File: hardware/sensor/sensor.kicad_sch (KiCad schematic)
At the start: 35 parts, among them IC1 ATTINY202-SSN, IC2 Si4012-C1001GTR, IC3 TPS3839L30DBZR, J1 M20-9770342

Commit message: EG-22 All components places frozen. No connections yet.
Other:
- moved on the sheet: ANT1
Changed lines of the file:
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@@
 	)
 	(junction
+		(at 59.69 34.29)
+		(diameter 0)
+		(color 0 0 0 0)
+	)
+	(junction
 		(at 73.66 36.83)
 		(diameter 0)
@@
 	)
 	(junction
+		(at 59.69 171.45)
+		(diameter 0)
+		(color 0 0 0 0)
+	)
+	(junction
 		(at 119.38 129.54)
 		(diameter 0)
@@
 	)
 	(junction
-		(at 59.69 171.45)
-		(diameter 0)
-		(color 0 0 0 0)
-	)
-	(junction
 		(at 143.51 140.97)
 		(diameter 0)
@@
 	)
 	(junction
-		(at 48.26 34.29)
-		(diameter 0)
-		(color 0 0 0 0)
-	)
-	(junction
 		(at 149.86 93.98)
 		(diameter 0)
@@
 	)
 	(no_connect
+		(at 52.07 173.99)
+	)
+	(no_connect
 		(at 186.69 99.06)
 	)
@@
 		(at 158.75 88.9)
 	)
-	(no_connect
-		(at 52.07 168.91)
-	)
 	(wire
 		(pts
@@
 	(wire
 		(pts
+			(xy 52.07 171.45) (xy 59.69 171.45)
+		)
+		(stroke
+			(width 0)
+			(type default)
+		)
+	)
+	(wire
+		(pts
 			(xy 111.76 129.54) (xy 119.38 129.54)
 		)
@@
 	(wire
 		(pts
+			(xy 59.69 34.29) (xy 59.69 54.61)
+		)
+		(stroke
+			(width 0)
+			(type default)
+		)
+	)
+	(wire
+		(pts
 			(xy 204.47 78.74) (xy 204.47 88.9)
 		)
@@
 	(wire
 		(pts
+			(xy 59.69 34.29) (xy 66.04 34.29)
+		)
+		(stroke
+			(width 0)
+			(type default)
+		)
+	)
+	(wire
+		(pts
 			(xy 119.38 140.97) (xy 119.38 171.45)
 		)
@@
 	(wire
 		(pts
-			(xy 41.91 34.29) (xy 48.26 34.29)
-		)
-		(stroke
-			(width 0)
-			(type default)
-		)
-	)
-	(wire
-		(pts
 			(xy 151.13 124.46) (xy 151.13 132.08)
 		)
@@
 	(wire
 		(pts
-			(xy 48.26 34.29) (xy 66.04 34.29)
+			(xy 41.91 34.29) (xy 59.69 34.29)
 		)
 		(stroke
@@
 	(wire
 		(pts
-			(xy 48.26 34.29) (xy 48.26 49.53)
-		)
-		(stroke
-			(width 0)
-			(type default)
-		)
-	)
-	(wire
-		(pts
 			(xy 242.57 38.1) (xy 248.92 38.1)
 		)
@@
 	(wire
 		(pts
-			(xy 52.07 171.45) (xy 59.69 171.45)
-		)
-		(stroke
-			(width 0)
-			(type default)
-		)
-	)
-	(wire
-		(pts
 			(xy 254 92.71) (xy 254 105.41)
 		)
@@
 	(symbol
 		(lib_id "power:GND")
-		(at 48.26 49.53 0)
-		(unit 1)
-		(exclude_from_sim no)
-		(in_bom yes)
-		(on_board yes)
-		(dnp no)
-		(fields_autoplaced yes)
-		(property "Reference" "#PWR031"
-			(at 48.26 55.88 0)
-			(effects
-				(font
-					(size 1.27 1.27)
-				)
-				(hide yes)
-			)
-		)
-		(property "Value" "GND"
-			(at 48.26 54.61 0)
-			(effects
-				(font
-					(size 1.27 1.27)
-				)
-				(hide yes)
-			)
-		)
-		(property "Footprint" ""
-			(at 48.26 49.53 0)
-			(effects
-				(font
-					(size 1.27 1.27)
-				)
-				(hide yes)
-			)
-		)
-		(property "Datasheet" ""
-			(at 48.26 49.53 0)
-			(effects
-				(font
-					(size 1.27 1.27)
-				)
-				(hide yes)
-			)
-		)
-		(property "Description" "Power symbol creates a global label with name \"GND\" , ground"
-			(at 48.26 49.53 0)
-			(effects
-				(font
-					(size 1.27 1.27)
-				)
-				(hide yes)
-			)
-		)
-		(pin "1"
-		)
-		(instances
-			(project "sensor"
-				(path "/0111ad26-080c-47bf-9fe6-1fe36fa86fb2"
-					(reference "#PWR031")
-					(unit 1)
-				)
-			)
-		)
-	)
-	(symbol
-		(lib_id "power:GND")
 		(at 204.47 118.11 0)
 		(unit 1)
@@
 	(symbol
 		(lib_id "ANT-868-HESM:ANT-868-HESM")
-		(at 52.07 171.45 180)
+		(at 52.07 171.45 0)
+		(mirror y)
 		(unit 1)
 		(exclude_from_sim no)
@@
 		(on_board yes)
 		(dnp no)
-		(fields_autoplaced yes)
 		(property "Reference" "ANT1"
-			(at 41.91 161.29 0)
+			(at 41.91 181.61 0)
 			(effects
 				(font
@@
 		)
 		(property "Value" "ANT-868-HESM"
-			(at 41.91 163.83 0)
+			(at 41.91 179.07 0)
 			(effects
 				(font
@@
 		)
 		(property "Footprint" "MyParts:ANT-868-HESM"
-			(at 35.56 76.53 0)
+			(at 35.56 266.37 0)
 			(effects
 				(font
@@
 		)
 		(property "Datasheet" "https://www.te.com/commerce/DocumentDelivery/DDEController?Action=showdoc&DocId=Data+Sheet%7Fant-868-hexx%7FA%7Fpdf%7FEnglish%7FENG_DS_ant-868-hexx_A.pdf%7FANT-868-HETH"
-			(at 35.56 -23.47 0)
+			(at 35.56 366.37 0)
 			(effects
 				(font
@@
 		)
 		(property "Height" "8.9"
-			(at 35.56 -223.47 0)
+			(at 35.56 566.37 0)
 			(effects
 				(font
@@
 		)
 		(property "Mouser Part Number" "712-ANT-868-HESM"
-			(at 35.56 -323.47 0)
+			(at 35.56 666.37 0)
 			(effects
 				(font
@@
 		)
 		(property "Mouser Price/Stock" "https://pt.mouser.com/ProductDetail/TE-Connectivity-Linx-Technologies/ANT-868-HESM?qs=hWgE7mdIu5TTyqPbNERfhg%3D%3D"
-			(at 35.56 -423.47 0)
+			(at 35.56 766.37 0)
 			(effects
 				(font
@@
 		)
 		(property "Manufacturer_Name" "TE Connectivity"
-			(at 35.56 -523.47 0)
+			(at 35.56 866.37 0)
 			(effects
 				(font
@@
 		)
 		(property "Manufacturer_Part_Number" "ANT-868-HETH"
-			(at 35.56 -623.47 0)
+			(at 35.56 966.37 0)
 			(effects
 				(font
@@
 					(unit 1)
 				)
+			)
+		)
+	)
+	(symbol
+		(lib_id "power:GND")
+		(at 59.69 54.61 0)
+		(unit 1)
+		(exclude_from_sim no)
+		(in_bom yes)
+		(on_board yes)
+		(dnp no)
+		(fields_autoplaced yes)
+		(property "Reference" "#PWR034"
+			(at 59.69 60.96 0)
+			(effects
+				(font
+					(size 1.27 1.27)
+				)
+				(hide yes)
+			)
+		)
+		(property "Value" "GND"
+			(at 59.69 59.69 0)
+			(effects
+				(font
+					(size 1.27 1.27)
+				)
+				(hide yes)
+			)
+		)
+		(property "Footprint" ""
+			(at 59.69 54.61 0)
+			(effects
+				(font
+					(size 1.27 1.27)
+				)
+				(hide yes)
+			)
+		)
+		(property "Datasheet" ""
+			(at 59.69 54.61 0)
+			(effects
+				(font
+					(size 1.27 1.27)
+				)
+				(hide yes)
+			)
+		)
+		(property "Description" "Power symbol creates a global label with name \"GND\" , ground"
+			(at 59.69 54.61 0)
+			(effects
+				(font
+					(size 1.27 1.27)
+				)
+				(hide yes)
+			)
+		)
+		(pin "1"
+		)
+		(instances
+			(project "sensor"
+				(path "/0111ad26-080c-47bf-9fe6-1fe36fa86fb2"
+					(reference "#PWR034")
+					(unit 1)
+				)

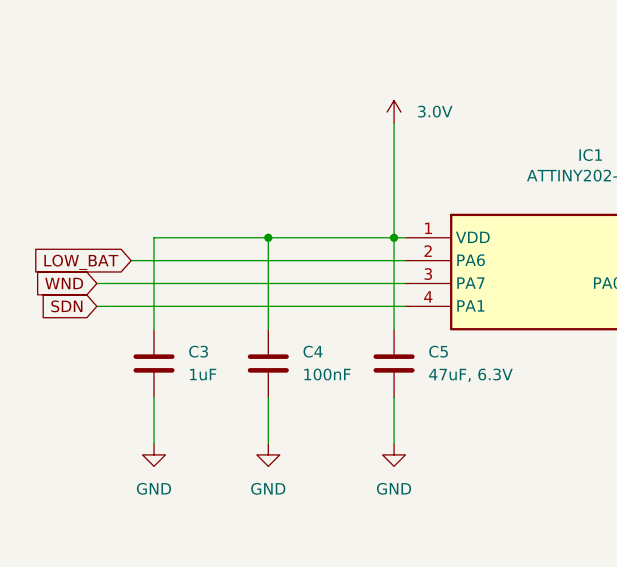
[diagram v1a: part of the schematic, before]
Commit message: EG-22 All Components connected, except ground and VDD, RF_VDD planes and CPWG to antenna.
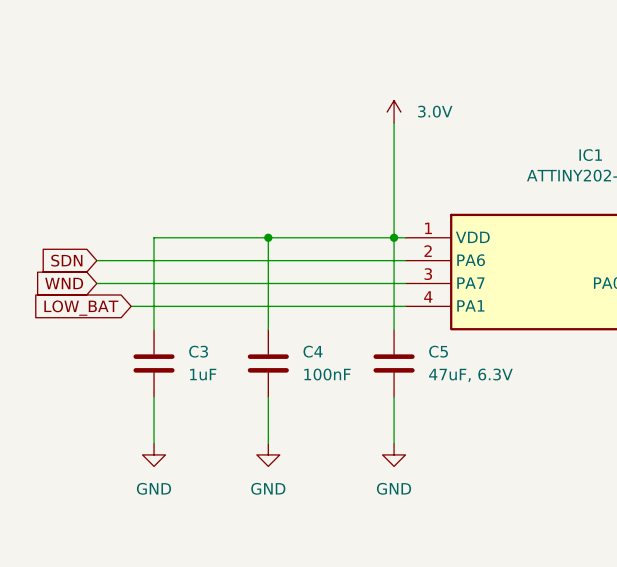
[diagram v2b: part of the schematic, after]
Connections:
- net LOW_BAT: now also IC1.4 (PA1); no longer IC1.2 (PA6)
- net SDN: now also IC1.2 (PA6); no longer IC1.4 (PA1)

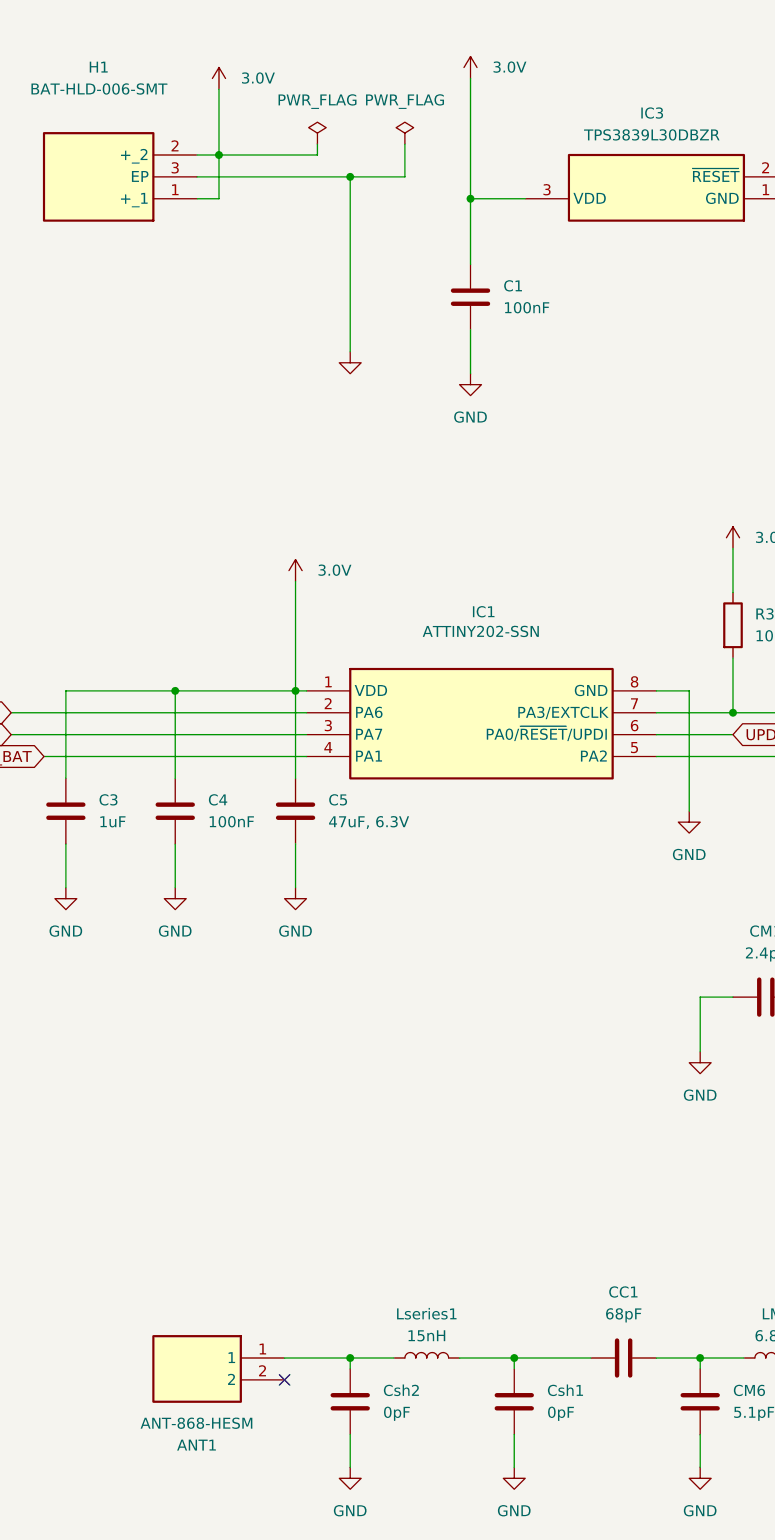
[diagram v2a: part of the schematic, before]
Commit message: EG-22 All connections, including antenna path and ground planes. Only vias are missing between groud planes.
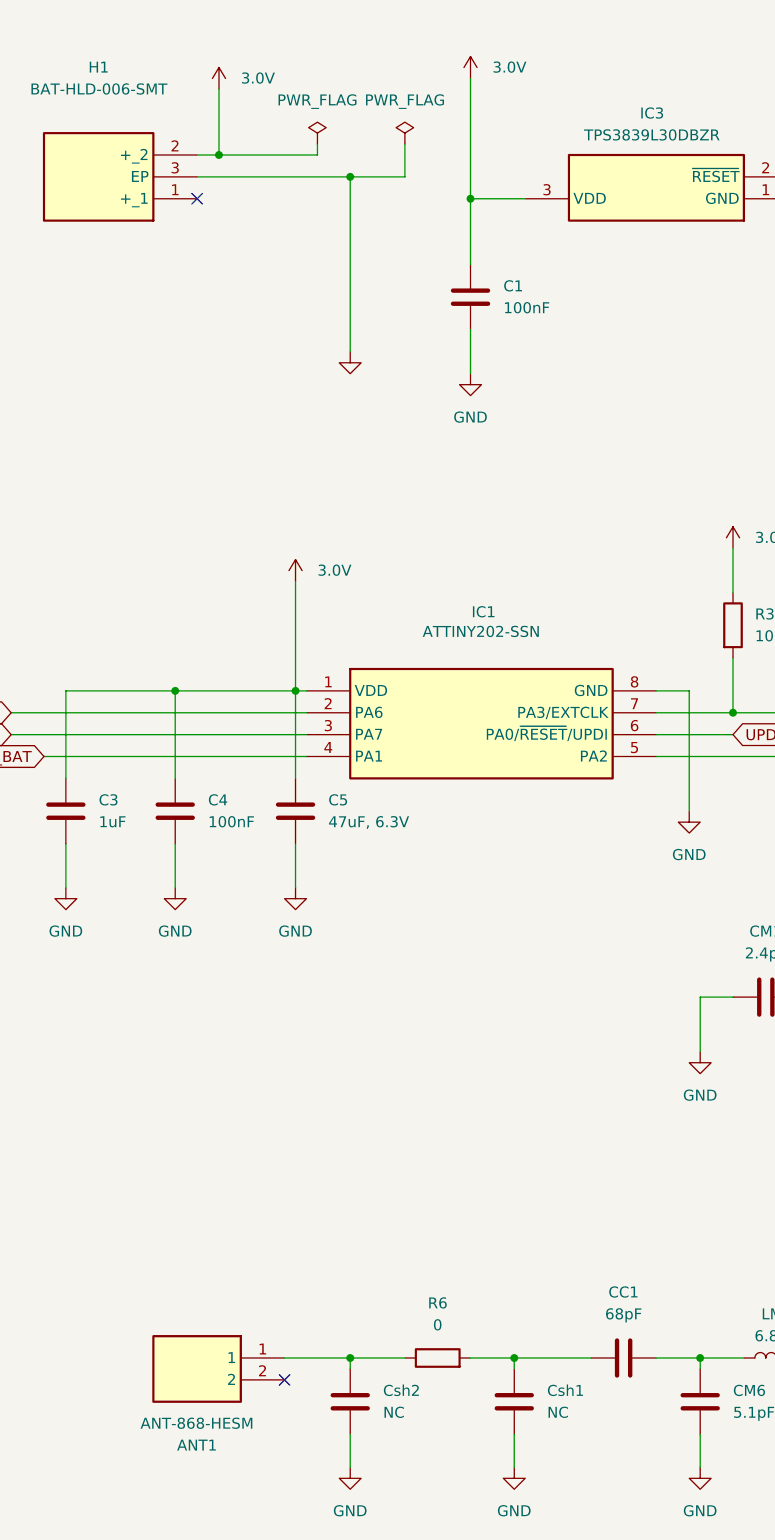
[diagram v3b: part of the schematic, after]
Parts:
- removed Lseries1: 15nH, Inductor_SMD:L_0402_1005Metric, symbol Device:L
- added R6: 0, Resistor_SMD:R_0603_1608Metric, symbol Device:R
- Csh1: value 0pF -> NC; footprint Capacitor_SMD:C_0402_1005Metric -> Capacitor_SMD:C_0603_1608Metric; DNP (none) -> NO
- Csh2: value 0pF -> NC; footprint Capacitor_SMD:C_0402_1005Metric -> Capacitor_SMD:C_0603_1608Metric; Populate (none) -> NO
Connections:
- net 3.0V: no longer H1.1 (+_1)
- net at ANT1.1, Csh2.1: now also R6.1
- net at CC1.1, Csh1.1: now also R6.2
- no-connect marks 4 -> 5
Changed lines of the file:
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@@
 	)
 	(junction
-		(at 59.69 171.45)
-		(diameter 0)
-		(color 0 0 0 0)
-	)
-	(junction
 		(at 119.38 129.54)
 		(diameter 0)
@@
 	)
 	(junction
+		(at 59.69 171.45)
+		(diameter 0)
+		(color 0 0 0 0)
+	)
+	(junction
 		(at 113.03 101.6)
 		(diameter 0)
@@
 		(at 158.75 88.9)
 	)
+	(no_connect
+		(at 41.91 36.83)
+	)
 	(wire
 		(pts
@@
 	(wire
 		(pts
-			(xy 72.39 171.45) (xy 78.74 171.45)
-		)
-		(stroke
-			(width 0)
-			(type default)
-		)
-	)
-	(wire
-		(pts
 			(xy 119.38 171.45) (xy 119.38 172.72)
 		)
@@
 	(wire
 		(pts
+			(xy 73.66 171.45) (xy 78.74 171.45)
+		)
+		(stroke
+			(width 0)
+			(type default)
+		)
+	)
+	(wire
+		(pts
 			(xy 53.34 81.28) (xy 53.34 93.98)
 		)
@@
 	(wire
 		(pts
-			(xy 44.45 36.83) (xy 44.45 31.75)
-		)
-		(stroke
-			(width 0)
-			(type default)
-		)
-	)
-	(wire
-		(pts
 			(xy 73.66 44.45) (xy 73.66 36.83)
 		)
@@
 	(wire
 		(pts
-			(xy 41.91 36.83) (xy 44.45 36.83)
-		)
-		(stroke
-			(width 0)
-			(type default)
-		)
-	)
-	(wire
-		(pts
 			(xy 104.14 90.17) (xy 104.14 96.52)
 		)
@@
 	(wire
 		(pts
+			(xy 59.69 171.45) (xy 66.04 171.45)
+		)
+		(stroke
+			(width 0)
+			(type default)
+		)
+	)
+	(wire
+		(pts
 			(xy 95.25 101.6) (xy 113.03 101.6)
 		)
@@
 	(wire
 		(pts
-			(xy 59.69 171.45) (xy 64.77 171.45)
-		)
-		(stroke
-			(width 0)
-			(type default)
-		)
-	)
-	(wire
-		(pts
 			(xy 149.86 78.74) (xy 149.86 82.55)
 		)
@@
 	)
 	(symbol
-		(lib_id "Device:L")
-		(at 68.58 171.45 90)
-		(unit 1)
-		(exclude_from_sim no)
-		(in_bom yes)
-		(on_board yes)
-		(dnp no)
-		(fields_autoplaced yes)
-		(property "Reference" "Lseries1"
-			(at 68.58 166.37 90)
-			(effects
-				(font
-					(size 1.27 1.27)
-				)
-			)
-		)
-		(property "Value" "15nH"
-			(at 68.58 168.91 90)
-			(effects
-				(font
-					(size 1.27 1.27)
-				)
-			)
-		)
-		(property "Footprint" "Inductor_SMD:L_0402_1005Metric"
-			(at 68.58 171.45 0)
-			(effects
-				(font
-					(size 1.27 1.27)
-				)
-				(hide yes)
-			)
-		)
-		(property "Datasheet" "~"
-			(at 68.58 171.45 0)
-			(effects
-				(font
-					(size 1.27 1.27)
-				)
-				(hide yes)
-			)
-		)
-		(property "Description" "Inductor"
-			(at 68.58 171.45 0)
-			(effects
-				(font
-					(size 1.27 1.27)
-				)
-				(hide yes)
-			)
-		)
-		(property "Mouser Part Number" "994-0402HP-15NXJRW"
-			(at 68.58 171.45 0)
-			(effects
-				(font
-					(size 1.27 1.27)
-				)
-				(hide yes)
-			)
-		)
-		(property "Mouser Price/Stock" "https://eu.mouser.com/ProductDetail/Coilcraft/0402HP-15NXJRW?qs=QNEnbhJQKvYIHcbZYhY5ig%3D%3D"
-			(at 68.58 171.45 0)
-			(effects
-				(font
-					(size 1.27 1.27)
-				)
-				(hide yes)
-			)
-		)
-		(property "Manufacturer_Name" "Coilcraft"
-			(at 68.58 171.45 0)
-			(effects
-				(font
-					(size 1.27 1.27)
-				)
-				(hide yes)
-			)
-		)
-		(property "Manufacturer_Part_Number" "0402HP-15NXJRW "
-			(at 68.58 171.45 0)
-			(effects
-				(font
-					(size 1.27 1.27)
-				)
-				(hide yes)
-			)
-		)
-		(pin "1"
-		)
-		(pin "2"
-		)
-		(instances
-			(project "sensor"
-				(path "/0111ad26-080c-47bf-9fe6-1fe36fa86fb2"
-					(reference "Lseries1")
-					(unit 1)
-				)
-			)
-		)
-	)
-	(symbol
 		(lib_id "Device:C")
 		(at 119.38 176.53 0)
@@
 			)
 		)
-		(property "Value" "0pF"
+		(property "Value" "NC"
 			(at 82.55 177.7999 0)
 			(effects
@@
 			)
 		)
-		(property "Footprint" "Capacitor_SMD:C_0402_1005Metric"
+		(property "Footprint" "Capacitor_SMD:C_0603_1608Metric"
 			(at 79.7052 180.34 0)
 			(effects
@@
 			)
 		)
+		(property "DNP" "NO"
+			(at 78.74 176.53 0)
+			(effects
+				(font
+					(size 1.27 1.27)
+				)
+				(hide yes)
+			)
+		)
 		(pin "1"
 		)
@@
 	)
 	(symbol
+		(lib_id "Device:R")
+		(at 69.85 171.45 90)
+		(unit 1)
+		(exclude_from_sim no)
+		(in_bom yes)
+		(on_board yes)
+		(dnp no)
+		(fields_autoplaced yes)
+		(property "Reference" "R6"
+			(at 69.85 165.1 90)
+			(effects
+				(font
+					(size 1.27 1.27)
+				)
+			)
+		)
+		(property "Value" "0"
+			(at 69.85 167.64 90)
+			(effects
+				(font
+					(size 1.27 1.27)
+				)
+			)
+		)
+		(property "Footprint" "Resistor_SMD:R_0603_1608Metric"
+			(at 69.85 173.228 90)
+			(effects
+				(font
+					(size 1.27 1.27)
+				)
+				(hide yes)
+			)
+		)
+		(property "Datasheet" "~"
+			(at 69.85 171.45 0)
+			(effects
+				(font
+					(size 1.27 1.27)
+				)
+				(hide yes)
+			)
+		)
+		(property "Description" "Resistor"
+			(at 69.85 171.45 0)
+			(effects
+				(font
+					(size 1.27 1.27)
+				)
+				(hide yes)
+			)
+		)
+		(property "Mouser Part Number" "71-CRCW0603-0-E3"
+			(at 69.85 171.45 90)
+			(effects
+				(font
+					(size 1.27 1.27)
+				)
+				(hide yes)
+			)
+		)
+		(property "Mouser Price/Stock" "https://pt.mouser.com/ProductDetail/Vishay/CRCW06030000Z0EA?qs=sGAEpiMZZMvdGkrng054t1X0qgDPqELU%252B4gm%252BoQ%252B0vM%3D"
+			(at 69.85 171.45 90)
+			(effects
+				(font
+					(size 1.27 1.27)
+				)
+				(hide yes)
+			)
+		)
+		(property "Manufacturer_Name" "Vishay"
+			(at 69.85 171.45 90)
+			(effects
+				(font
+					(size 1.27 1.27)
+				)
+				(hide yes)
+			)
+		)
+		(property "Manufacturer_Part_Number" "CRCW06030000Z0EA"
+			(at 69.85 171.45 90)
+			(effects
+				(font
+					(size 1.27 1.27)
+				)
+				(hide yes)
+			)
+		)
+		(pin "1"
+		)
+		(pin "2"
+		)
+		(instances
+			(project ""
+				(path "/0111ad26-080c-47bf-9fe6-1fe36fa86fb2"
+					(reference "R6")
+					(unit 1)
+				)
+			)
+		)
+	)
+	(symbol
 		(lib_id "power:VDD")
 		(at 171.45 17.78 0)
@@
 			)
 		)
-		(property "Value" "0pF"
+		(property "Value" "NC"
 			(at 63.5 177.7999 0)
 			(effects
@@
 			)
 		)
-		(property "Footprint" "Capacitor_SMD:C_0402_1005Metric"
+		(property "Footprint" "Capacitor_SMD:C_0603_1608Metric"
 			(at 60.6552 180.34 0)
 			(effects
@@
 			(at 59.69 176.53 0)
 			(effects
+				(font
+					(size 1.27 1.27)
+				)
+				(hide yes)
+			)
+		)
+		(property "Populate" "NO"
+			(at 59.69 176.53 0)
+			(effects
